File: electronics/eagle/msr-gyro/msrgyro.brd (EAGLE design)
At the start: 25 x 25 mm, 24 parts, among them IC1 LSM6DS3TR-C, IC2 STM32G030F6P6, J1 JD, J2 PWR, J3 GND, J4 GND, J6 HACK-CONNECT-5, U2 XC6206-SOT23-3

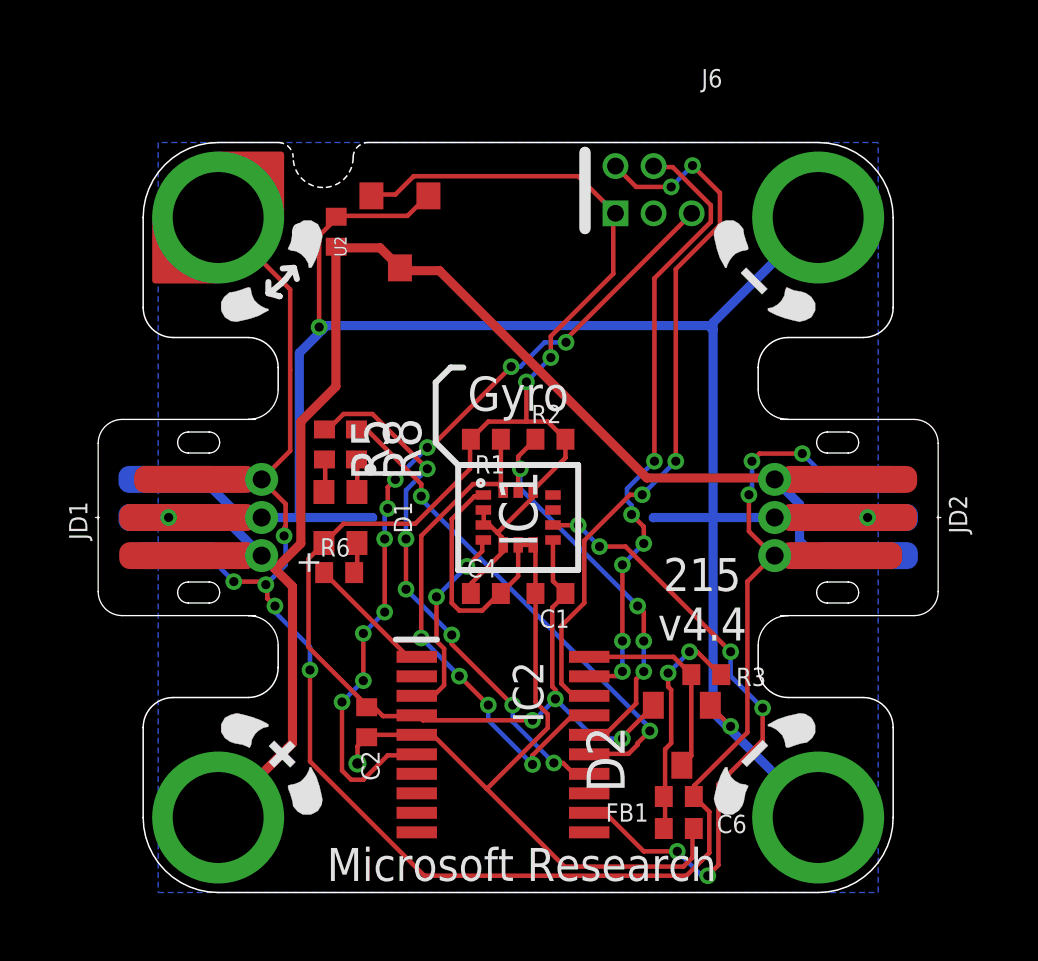
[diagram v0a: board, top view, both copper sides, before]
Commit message: rotate LSM6D to match JLC spec
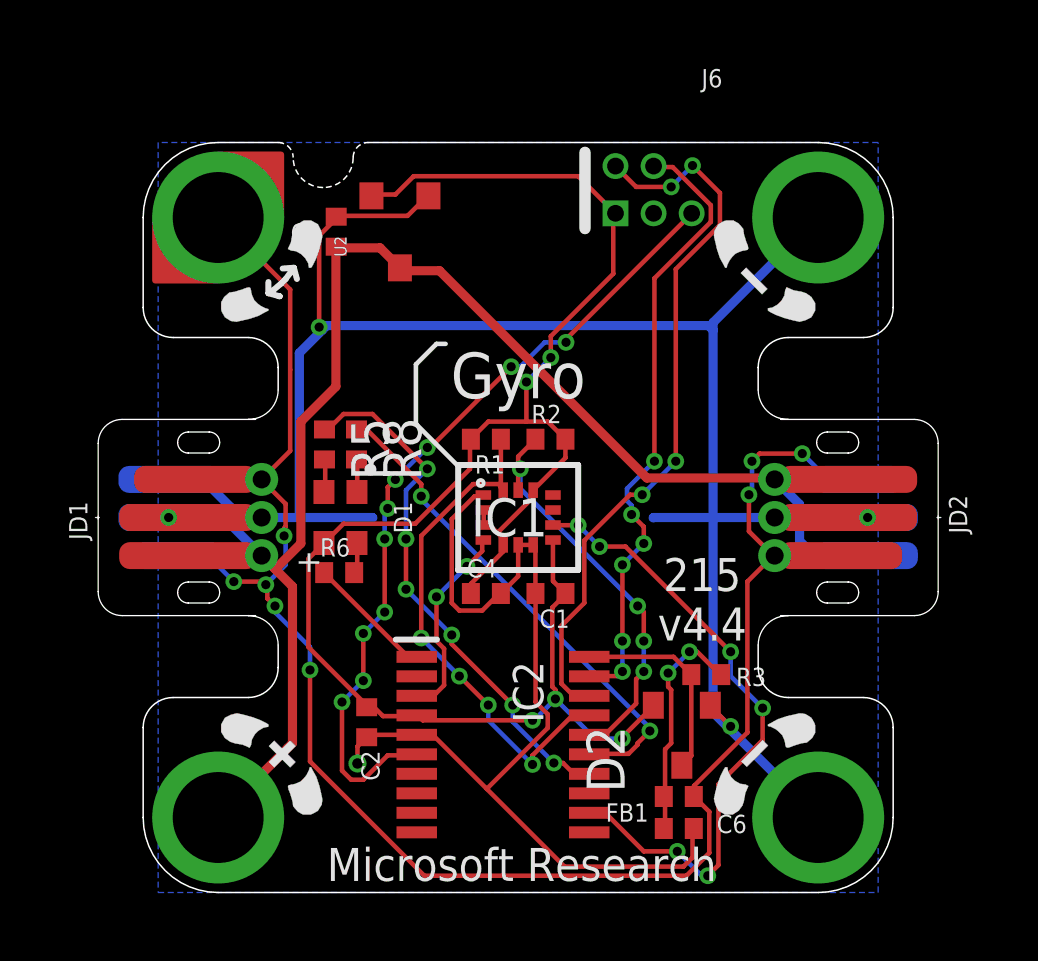
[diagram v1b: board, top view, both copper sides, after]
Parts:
- turned IC1 to 0 degrees
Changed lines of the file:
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@@
 <grid distance="3" unitdist="mil" unit="mil" style="lines" multiple="1" display="yes" altdistance="25" altunitdist="mil" altunit="mil"/>
 <layers>
-<layer number="1" name="Top" color="4" fill="1" visible="yes" active="yes"/>
-<layer number="16" name="Bottom" color="1" fill="1" visible="yes" active="yes"/>
+<layer number="1" name="Top" color="4" fill="1" visible="no" active="yes"/>
+<layer number="16" name="Bottom" color="1" fill="1" visible="no" active="yes"/>
 <layer number="17" name="Pads" color="2" fill="1" visible="yes" active="yes"/>
 <layer number="18" name="Vias" color="2" fill="1" visible="yes" active="yes"/>
@@
 <layer number="20" name="Dimension" color="11" fill="1" visible="yes" active="yes"/>
 <layer number="21" name="tPlace" color="7" fill="1" visible="yes" active="yes"/>
-<layer number="22" name="bPlace" color="7" fill="1" visible="yes" active="yes"/>
+<layer number="22" name="bPlace" color="7" fill="1" visible="no" active="yes"/>
 <layer number="23" name="tOrigins" color="15" fill="1" visible="yes" active="yes"/>
-<layer number="24" name="bOrigins" color="15" fill="1" visible="yes" active="yes"/>
+<layer number="24" name="bOrigins" color="15" fill="1" visible="no" active="yes"/>
 <layer number="25" name="tNames" color="7" fill="1" visible="no" active="yes"/>
 <layer number="26" name="bNames" color="7" fill="1" visible="no" active="yes"/>
 <layer number="27" name="tValues" color="7" fill="1" visible="no" active="yes"/>
 <layer number="28" name="bValues" color="7" fill="1" visible="no" active="yes"/>
-<layer number="29" name="tStop" color="7" fill="3" visible="no" active="yes"/>
+<layer number="29" name="tStop" color="7" fill="3" visible="yes" active="yes"/>
 <layer number="30" name="bStop" color="7" fill="6" visible="no" active="yes"/>
-<layer number="31" name="tCream" color="7" fill="4" visible="no" active="yes"/>
+<layer number="31" name="tCream" color="7" fill="4" visible="yes" active="yes"/>
 <layer number="32" name="bCream" color="7" fill="5" visible="no" active="yes"/>
 <layer number="33" name="tFinish" color="6" fill="3" visible="no" active="yes"/>
@@
 <layer number="37" name="tTest" color="7" fill="1" visible="no" active="yes"/>
 <layer number="38" name="bTest" color="7" fill="1" visible="no" active="yes"/>
-<layer number="39" name="tKeepout" color="4" fill="11" visible="yes" active="yes"/>
-<layer number="40" name="bKeepout" color="1" fill="11" visible="yes" active="yes"/>
+<layer number="39" name="tKeepout" color="4" fill="11" visible="no" active="yes"/>
+<layer number="40" name="bKeepout" color="1" fill="11" visible="no" active="yes"/>
 <layer number="41" name="tRestrict" color="4" fill="10" visible="no" active="yes"/>
 <layer number="42" name="bRestrict" color="1" fill="10" visible="no" active="yes"/>
 <layer number="43" name="vRestrict" color="2" fill="10" visible="no" active="yes"/>
 <layer number="44" name="Drills" color="7" fill="1" visible="no" active="yes"/>
-<layer number="45" name="Holes" color="7" fill="1" visible="no" active="yes"/>
+<layer number="45" name="Holes" color="7" fill="1" visible="yes" active="yes"/>
 <layer number="46" name="Milling" color="3" fill="1" visible="yes" active="yes"/>
 <layer number="47" name="Measures" color="7" fill="1" visible="no" active="yes"/>
@@
 <layer number="50" name="dxf" color="7" fill="1" visible="no" active="yes"/>
 <layer number="51" name="tDocu" color="25" fill="1" visible="yes" active="yes"/>
-<layer number="52" name="bDocu" color="25" fill="1" visible="yes" active="yes"/>
+<layer number="52" name="bDocu" color="25" fill="1" visible="no" active="yes"/>
 <layer number="90" name="Modules" color="5" fill="1" visible="no" active="no"/>
 <layer number="91" name="Nets" color="2" fill="1" visible="no" active="no"/>
@@
 Research
 Gyro</text>
-<text x="14.0012" y="16.6274" size="1.143" layer="21" font="vector" ratio="13" align="center">Gyro
+<text x="14.0012" y="17.237" size="1.524" layer="21" font="vector" ratio="13" align="center">Gyro
 </text>
 <wire x1="4" y1="0" x2="24" y2="0" width="0.05" layer="20"/>
@@
 <wire x1="16" y1="10.75" x2="12" y2="10.75" width="0.2" layer="21"/>
 <wire x1="12" y1="10.75" x2="12" y2="14.25" width="0.2" layer="21"/>
-<wire x1="12.1738" y1="17.5" x2="11.75" y2="17.5" width="0.2" layer="21"/>
-<wire x1="11.75" y1="17.5" x2="11.25" y2="17" width="0.2" layer="21"/>
-<wire x1="11.25" y1="17" x2="11.25" y2="15" width="0.2" layer="21"/>
-<wire x1="11.25" y1="15" x2="12" y2="14.25" width="0.2" layer="21"/>
 <text x="20.1374" y="9.7744" size="1.1" layer="21" font="vector" ratio="10" align="center">215
 v4.4</text>
 <text x="13.7548" y="2.508" size="1.397" layer="22" font="vector" ratio="10" rot="MR180" align="center">215 v4.4</text>
+<wire x1="12.0396" y1="14.1732" x2="10.5918" y2="15.621" width="0.1524" layer="21"/>
+<wire x1="10.5918" y1="15.621" x2="10.5918" y2="17.6022" width="0.1524" layer="21"/>
+<wire x1="10.5918" y1="17.6022" x2="11.2776" y2="18.288" width="0.1524" layer="21"/>
+<wire x1="11.2776" y1="18.288" x2="11.5824" y2="18.288" width="0.1524" layer="21"/>
 </plain>
 <attributes>
@@
 <attribute name="VALUE" x="14.4412" y="13.7046" size="0.8128" layer="27" ratio="10"/>
 </element>
-<element name="IC1" library="jacdac" package="LGA-14-2.5_3" value="LSM6DS3TR-C" x="14" y="12.5" smashed="yes" rot="R270">
-<attribute name="NAME" x="14.006" y="12.79" size="1.27" layer="25" rot="R270" align="center"/>
-<attribute name="VALUE" x="14.006" y="12.79" size="1.27" layer="27" rot="R270" align="center"/>
+<element name="IC1" library="jacdac" package="LGA-14-2.5_3" value="LSM6DS3TR-C" x="14" y="12.5" smashed="yes">
+<attribute name="NAME" x="13.71" y="12.506" size="1.27" layer="25" align="center"/>
+<attribute name="VALUE" x="13.71" y="12.506" size="1.27" layer="27" align="center"/>
 </element>
 <element name="C1" library="jacdac" package="0402" value="100nF" x="15.0762" y="9.9666" smashed="yes" rot="R180">
